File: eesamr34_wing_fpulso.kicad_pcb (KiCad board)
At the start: 2 copper layers, 50 x 24.9 mm, 19 parts, among them J3 Conn_01x02_Male, P1 SolderJumper_3_Bridged12, Q1 BS250, U2 4069

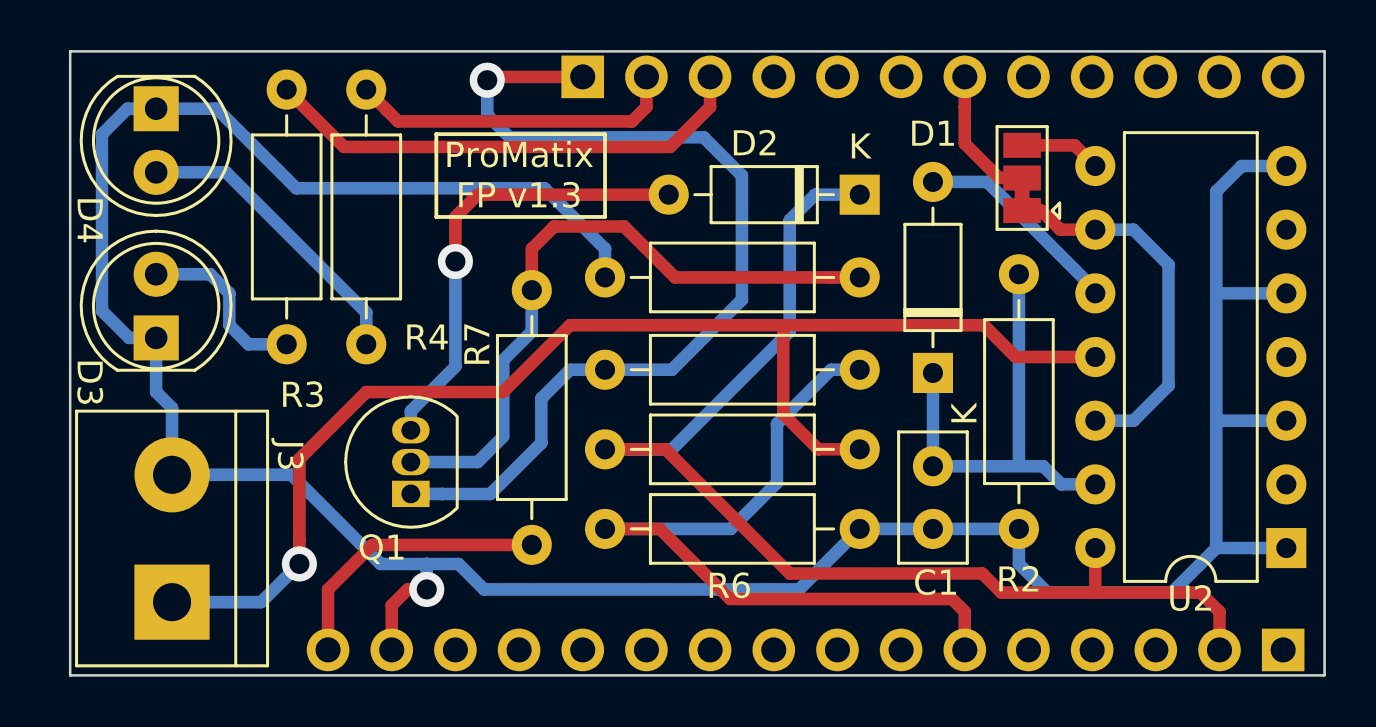
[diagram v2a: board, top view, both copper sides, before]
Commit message: quitado vbat to vcc y actualizado PCB
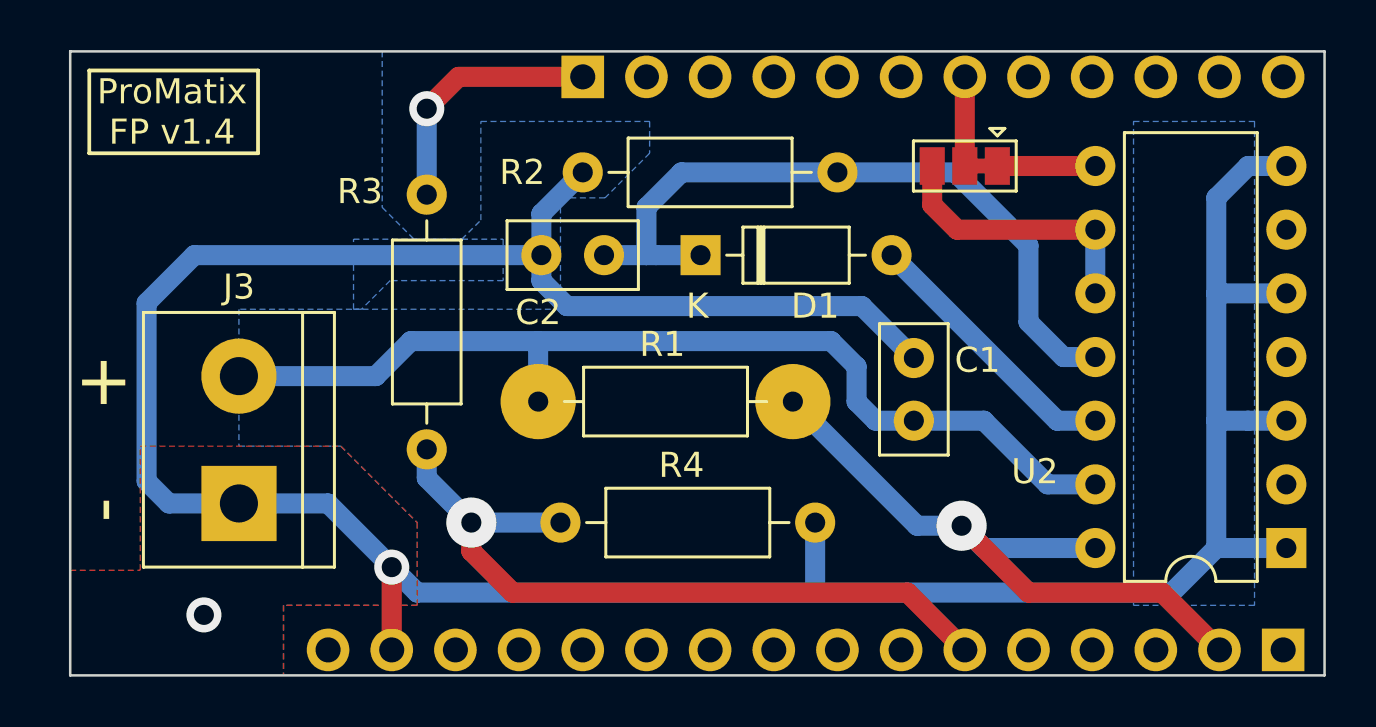
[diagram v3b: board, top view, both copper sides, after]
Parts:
- removed D2: 1N4148, Diode_THT:D_DO-35_SOD27_P7.62mm_Horizontal
- removed D3, D4: LED, LED_THT:LED_D5.0mm
- removed Q1: BS250, Package_TO_SOT_THT:TO-92_Inline
- removed R5: 330K, Resistor_THT:R_Axial_DIN0207_L6.3mm_D2.5mm_P10.16mm_Horizontal
- removed R6, R8: 100K, Resistor_THT:R_Axial_DIN0207_L6.3mm_D2.5mm_P10.16mm_Horizontal
- removed R7: 10K, Resistor_THT:R_Axial_DIN0207_L6.3mm_D2.5mm_P10.16mm_Horizontal
- added C2: 0.01uF, Capacitor_THT:C_Disc_D5.0mm_W2.5mm_P2.50mm, F.Cu at (95.3, 129.8)
- R1: value 330 ohms -> 39K
- R2: value 22Kohm -> 220Kohm
- R3: value 1K -> 330K
- R4: value 1K -> 100K
- moved R4 18.9 mm to (93.6, 140.5), turned to 0 degrees
- moved D1 10.4 mm to (99.2, 129.8), turned to 0 degrees
- moved R2 8.30 mm to (104.6, 126.5), turned to 180 degrees
- moved R1 7.73 mm to (102.9, 135.6), turned to 180 degrees
- moved R3 6.98 mm to (88.3, 127.4)
- moved J3 4.76 mm to (80.8, 139.7)
- moved P1 2.34 mm to (109.7, 126.2), turned to 180 degrees
- moved C1 1.97 mm to (107.7, 136.4), turned to 90 degrees
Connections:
- C1 pad 1: Net-(C1-Pad1) -> /Pulse
- D1 pad 1: Net-(C1-Pad1) -> Net-(C2-Pad1)
- J3 pad 1: /Pulse -> GND
- J3 pad 2: GND -> /Pulse
- JP1 pad 1: /BAND_SEL -> (no net)
- JP1 pad 10: /SPI_SCK -> (no net)
- JP1 pad 11: /SPI_SS -> (no net)
- JP1 pad 12: /PWM -> (no net)
- JP1 pad 13: /PA22 -> (no net)
- JP1 pad 14: /VDD_DIG -> (no net)
- JP1 pad 16: /VBUS -> (no net)
- JP1 pad 3: /VBATM -> (no net)
- JP1 pad 4: /UART_TX -> (no net)
- JP1 pad 5: /UART_RX -> (no net)
- JP1 pad 7: /SWDCLK -> (no net)
- JP1 pad 8: /VDD_CORE -> (no net)
- JP1 pad 9: /VSW -> (no net)
- JP3 pad 10: /PA27 -> (no net)
- JP3 pad 11: /ADC6 -> (no net)
- JP3 pad 12: /ADC7 -> (no net)
- JP3 pad 2: /PWMW2 -> (no net)
- JP3 pad 3: /I2C_SCL -> (no net)
- JP3 pad 4: /I2C_SDa -> (no net)
- JP3 pad 5: /PA14 -> (no net)
- JP3 pad 6: /PA15 -> (no net)
- JP3 pad 8: /TCXO -> (no net)
- JP3 pad 9: /PA08 -> (no net)
- R2 pad 1: Net-(C1-Pad1) -> Net-(C2-Pad1)
- R3 pad 1: /I2C_SCL -> /VBAT
- R3 pad 2: Net-(D3-Pad2) -> /SPI_MISO
- R4 pad 1: /PWMW2 -> /SPI_MISO
- R4 pad 2: Net-(D4-Pad2) -> GND
- U2 pad 10: Net-(D1-Pad2) -> Net-(P1-Pad3)
- U2 pad 11: /Pulse -> Net-(C2-Pad1)
- U2 pad 12: Net-(P1-Pad1) -> Net-(D1-Pad2)
- U2 pad 13: Net-(C1-Pad1) -> /Pulse
- U2 pad 2: Net-(U2-Pad2) -> (no net)
- U2 pad 4: Net-(U2-Pad4) -> (no net)
- U2 pad 6: Net-(U2-Pad6) -> (no net)
- U2 pad 8: Net-(P1-Pad3) -> Net-(P1-Pad1)
- U2 pad 9: Net-(P1-Pad1) -> Net-(P1-Pad3)
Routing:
- net Net-(C2-Pad1): track 0.00 -> 29.1 mm
- net /VBAT: track 38.8 -> 10.2 mm
- net Net-(Q1-Pad2): track 26.4 -> 0.00 mm
- net /+3.3V: track 47.5 -> 27.7 mm, vias 0 -> 1
- net /I2C_SCL: track 19.7 -> 0.00 mm
- net Net-(D2-Pad2): track 18.1 -> 0.00 mm, vias 1 -> 0
- net Net-(C1-Pad1): track 18.1 -> 0.00 mm
- net /PWMW2: track 13.1 -> 0.00 mm
- net Net-(D4-Pad2): track 12.0 -> 0.00 mm
- net /VBUS: track 11.3 -> 0.00 mm
- net /Pulse: track 51.6 -> 40.3 mm, vias 1 -> 0
- net Net-(P1-Pad1): track 15.1 -> 3.91 mm
- net Net-(P1-Pad3): track 3.26 -> 11.0 mm
- net Net-(D3-Pad2): track 7.11 -> 0.00 mm
- net GND: track 116.8 -> 121.8 mm, vias 1 -> 2
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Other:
- board text added: "+"
- board text added: "-"
- board text added: "ProMatix FP v1.4"
- board text removed: "ProMatix FP v1.3"

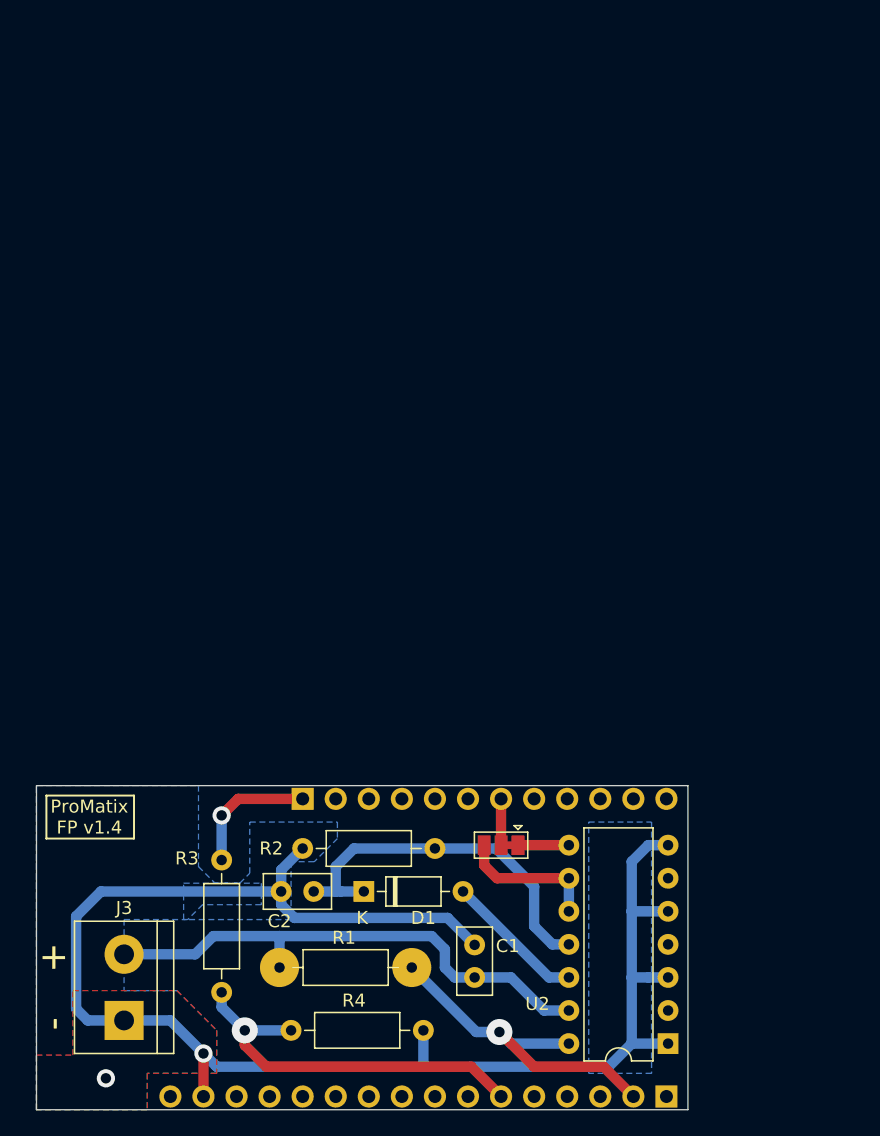
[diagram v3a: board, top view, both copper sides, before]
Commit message: Tercer borne permite alimentar el nodo usando 5v
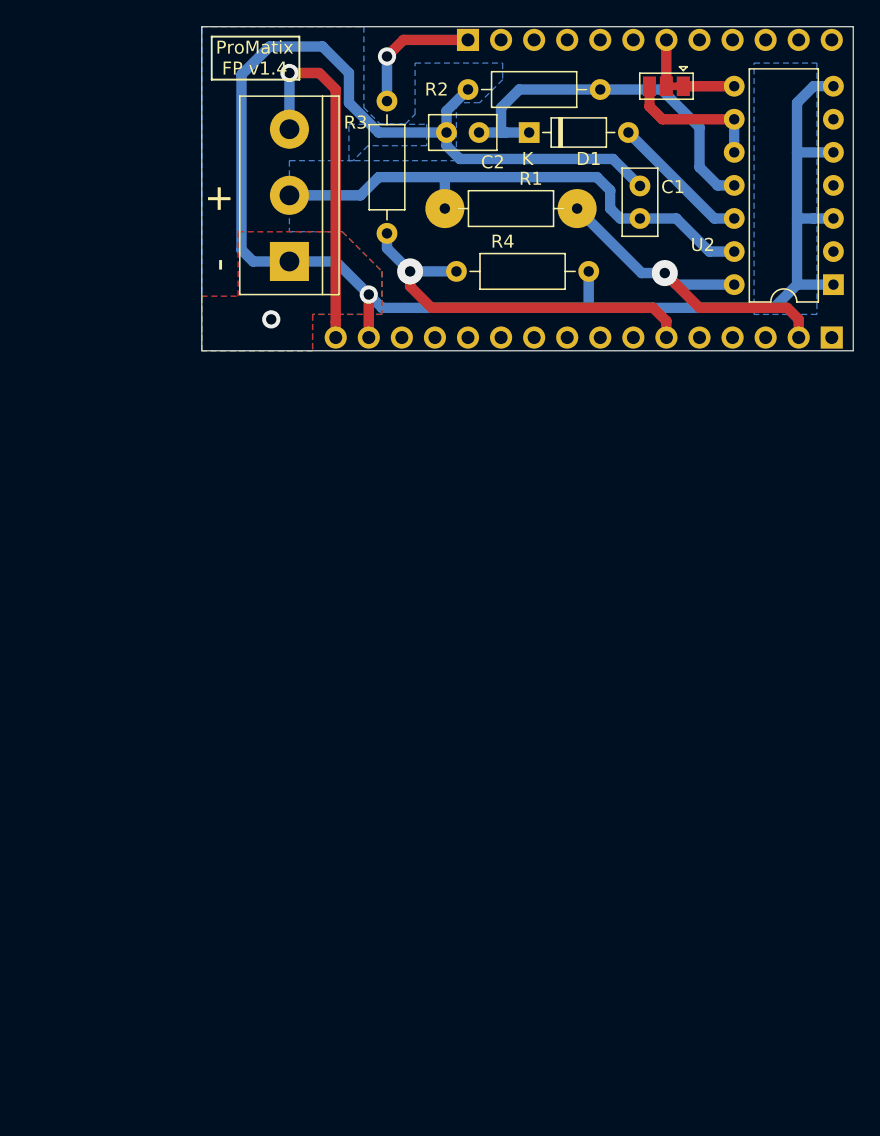
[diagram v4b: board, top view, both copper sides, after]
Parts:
- removed J3: Conn_01x02_Male, TerminalBlock:TerminalBlock_bornier-2_P5.08mm
- added J1: Conn_01x03_Male, TerminalBlock:TerminalBlock_bornier-3_P5.08mm, F.Cu at (93.5, 81.4)
- moved C2 59.7 mm to (108.0, 71.5)
- moved D1 59.7 mm to (111.9, 71.5)
- moved JP1 59.7 mm to (135.1, 87.2)
- moved JP3 59.7 mm to (107.2, 64.4)
- moved P1 59.7 mm to (122.4, 67.9)
- moved R2 59.7 mm to (117.3, 68.2)
- moved R3 59.7 mm to (101.0, 69.1)
- moved U2 59.7 mm to (135.3, 83.2)
- moved C1 59.7 mm to (120.4, 78.1)
- moved R1 59.7 mm to (115.6, 77.3)
- moved R4 59.7 mm to (106.3, 82.2)
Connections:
- JP1 pad 1: (no net) -> /BAND_SEL
- JP1 pad 10: (no net) -> /SPI_SCK
- JP1 pad 11: (no net) -> /SPI_SS
- JP1 pad 12: (no net) -> /PWM
- JP1 pad 13: (no net) -> /PA22
- JP1 pad 14: (no net) -> /VDD_DIG
- JP1 pad 16: (no net) -> /VBUS
- JP1 pad 3: (no net) -> /VBATM
- JP1 pad 4: (no net) -> /UART_TX
- JP1 pad 5: (no net) -> /UART_RX
- JP1 pad 7: (no net) -> /SWDCLK
- JP1 pad 8: (no net) -> /VDD_CORE
- JP1 pad 9: (no net) -> /VSW
- JP3 pad 10: (no net) -> /PA27
- JP3 pad 11: (no net) -> /ADC6
- JP3 pad 12: (no net) -> /ADC7
- JP3 pad 2: (no net) -> /PWMW2
- JP3 pad 3: (no net) -> /I2C_SCL
- JP3 pad 4: (no net) -> /I2C_SDa
- JP3 pad 5: (no net) -> /PA14
- JP3 pad 6: (no net) -> /PA15
- JP3 pad 8: (no net) -> /TCXO
- JP3 pad 9: (no net) -> /PA08
- U2 pad 2: (no net) -> Net-(U2-Pad2)
- U2 pad 4: (no net) -> Net-(U2-Pad4)
- U2 pad 6: (no net) -> Net-(U2-Pad6)
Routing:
- net /VBUS: track 0.00 -> 27.5 mm, vias 0 -> 1
- net GND: track 121.8 -> 132.3 mm
- net /+3.3V: track 27.7 -> 28.5 mm
- net /SPI_MISO: track 29.7 -> 30.4 mm
